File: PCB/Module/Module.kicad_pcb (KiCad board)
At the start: 2 copper layers, 30 x 30 mm, 22 parts, among them J1 SWD_Programmer, U1 PY32F002BF15P6TU, U2 PinHeaderTop, U3 PinHeaderRight, U4 PinHeaderBottom, U5 PinHeaderLeft, U6 Button

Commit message: Prevent accidental short circuit and add basic box 3d model freecad
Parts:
- moved R1 0.20 mm to (145.5, 91.2)
- moved R2 0.20 mm to (154.5, 91.2)
- moved R5 0.20 mm to (154.5, 108.8)
- moved R6 0.20 mm to (145.5, 108.8)
- moved R3 0.20 mm to (158.8, 95.5)
- moved R4 0.20 mm to (158.8, 104.5)
- moved R7 0.20 mm to (141.2, 104.5)
- moved R8 0.20 mm to (141.2, 95.5)
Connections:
- U2 pad 1: GND -> +5V
- U2 pad 2: +5V -> /DataTop1
- U2 pad 3: /DataTop1 -> GND
- U2 pad 4: /DataTop2 -> GND
- U2 pad 5: +5V -> /DataTop2
- U2 pad 6: GND -> +5V
- U3 pad 1: GND -> +5V
- U3 pad 2: +5V -> /DataRight1
- U3 pad 3: /DataRight1 -> GND
- U3 pad 4: /DataRight2 -> GND
- U3 pad 5: +5V -> /DataRight2
- U3 pad 6: GND -> +5V
- U4 pad 1: GND -> +5V
- U4 pad 2: +5V -> /DataBottom1
- U4 pad 3: /DataBottom1 -> GND
- U4 pad 4: /DataBottom2 -> GND
- U4 pad 5: +5V -> /DataBottom2
- U4 pad 6: GND -> +5V
- U5 pad 1: GND -> +5V
- U5 pad 2: +5V -> /DataLeft1
- U5 pad 3: /DataLeft1 -> GND
- U5 pad 4: /DataLeft2 -> GND
- U5 pad 5: +5V -> /DataLeft2
- U5 pad 6: GND -> +5V
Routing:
- net GND: track 37.3 -> 19.3 mm, vias 2 -> 5
- net +5V: track 14.3 -> 17.8 mm
- net /DataRight2: track 12.3 -> 11.8 mm
- net /DataRight1: track 12.3 -> 11.8 mm

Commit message: Update PCB
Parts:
- removed R9: 10k, Resistor_SMD:R_0402_1005Metric
- removed U6: Button, CustomFootprints:Button
- added J2: Shield_Connector_Top_Right, Connector_PinSocket_2.54mm:PinSocket_1x01_P2.54mm_Vertical, F.Cu at (161.0, 89.0)
- added J3: Shield_Connector_Bottom_Right, Connector_PinSocket_2.54mm:PinSocket_1x01_P2.54mm_Vertical, F.Cu at (161.0, 111.0)
- added J4: Shield_Connector_Top_Left, Connector_PinSocket_2.54mm:PinSocket_1x01_P2.54mm_Vertical, F.Cu at (139.0, 89.0)
- added J5: Shield_Connector_Bottom_Left, Connector_PinSocket_2.54mm:PinSocket_1x01_P2.54mm_Vertical, F.Cu at (139.0, 111.0)
- LED1, LED2, LED3, LED4: value LED-WS2812B -> SK6812MINI-HS; footprint CustomFootprints:LED-WS2812B -> CustomFootprints:LED-SK6812MINI-HS
- moved C1 16.1 mm to (145.3, 95.2), turned to 180 degrees
- moved R1 2.34 mm to (145.7, 93.5)
- moved R2 2.34 mm to (154.3, 93.5)
- moved R3 2.34 mm to (156.5, 95.7)
- moved R4 2.34 mm to (156.5, 104.3)
- moved U2 2.34 mm to (150.0, 91.5)
- moved U3 2.34 mm to (158.5, 100.0)
- moved U4 2.34 mm to (150.0, 108.5)
- moved U5 2.34 mm to (141.5, 100.0)
- moved R7 2.04 mm to (143.2, 104.3)
- moved R8 2.04 mm to (143.2, 95.7)
- moved R5 2.01 mm to (154.3, 106.8)
- moved R6 2.01 mm to (145.7, 106.8)
- moved C2 1.75 mm to (154.1, 105.1)
- moved LED2 1.10 mm to (155.4, 100.0), turned to 90 degrees
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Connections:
- LED1 pad 1: +5V -> GND
- LED1 pad 2: Net-(LED1-DOU) -> /LedIn
- LED1 pad 3: GND -> +5V
- LED1 pad 4: /LedIn -> Net-(LED1-DOUT)
- LED2 pad 1: +5V -> GND
- LED2 pad 2: Net-(LED2-DOU) -> Net-(LED1-DOUT)
- LED2 pad 3: GND -> +5V
- LED2 pad 4: Net-(LED1-DOU) -> Net-(LED2-DOUT)
- LED3 pad 1: +5V -> GND
- LED3 pad 2: Net-(LED3-DOU) -> Net-(LED2-DOUT)
- LED3 pad 3: GND -> +5V
- LED3 pad 4: Net-(LED2-DOU) -> Net-(LED3-DOUT)
- LED4 pad 1: +5V -> GND
- LED4 pad 2: unconnected-(LED4-DOU-Pad2) -> Net-(LED3-DOUT)
- LED4 pad 3: GND -> +5V
- LED4 pad 4: Net-(LED3-DOU) -> unconnected-(LED4-DOUT-Pad4)
- U1 pad 10: /DataRight1 -> /ShieldBottomRight
- U1 pad 12: unconnected-(U1-PB3-Pad12) -> /DataRight1
- U1 pad 13: unconnected-(U1-PB2-Pad13) -> /ShieldTopRight
- U1 pad 19: /ButtonRead -> /ShieldTopLeft
- U1 pad 2: unconnected-(U1-PA6-Pad2) -> /ShieldBottomLeft
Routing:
- net +5V: track 17.8 -> 87.3 mm, vias 2 -> 1
- net Net-(LED3-DOUT): track 0.00 -> 31.1 mm
- net Net-(LED2-DOUT): track 0.00 -> 31.0 mm
- net Net-(LED1-DOUT): track 0.00 -> 30.9 mm
- net /ShieldTopRight: track 0.00 -> 13.4 mm
- net /ShieldTopLeft: track 0.00 -> 13.1 mm
- net /ShieldBottomRight: track 0.00 -> 12.8 mm
- net /ShieldBottomLeft: track 0.00 -> 12.7 mm
- net /ButtonRead: track 10.7 -> 0.00 mm
- net Net-(LED1-DOU): track 8.95 -> 0.00 mm
- net Net-(LED3-DOU): track 8.95 -> 0.00 mm
- net GND: track 19.3 -> 12.2 mm, vias 5 -> 3
- net /DataLeft2: track 12.7 -> 5.96 mm
- net Net-(LED2-DOU): track 6.54 -> 0.00 mm
- net /DataLeft1: track 12.0 -> 5.96 mm
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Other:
- board size 30 x 30 mm -> 34.2 x 34.2 mm
- board text added: "+5V"
- board text added: "GND"
- board text added: "PCB"
- board text added: "Pogo Pins"
- board text added: "RST"
- board text added: "SWC"
- board text added: "SWD"

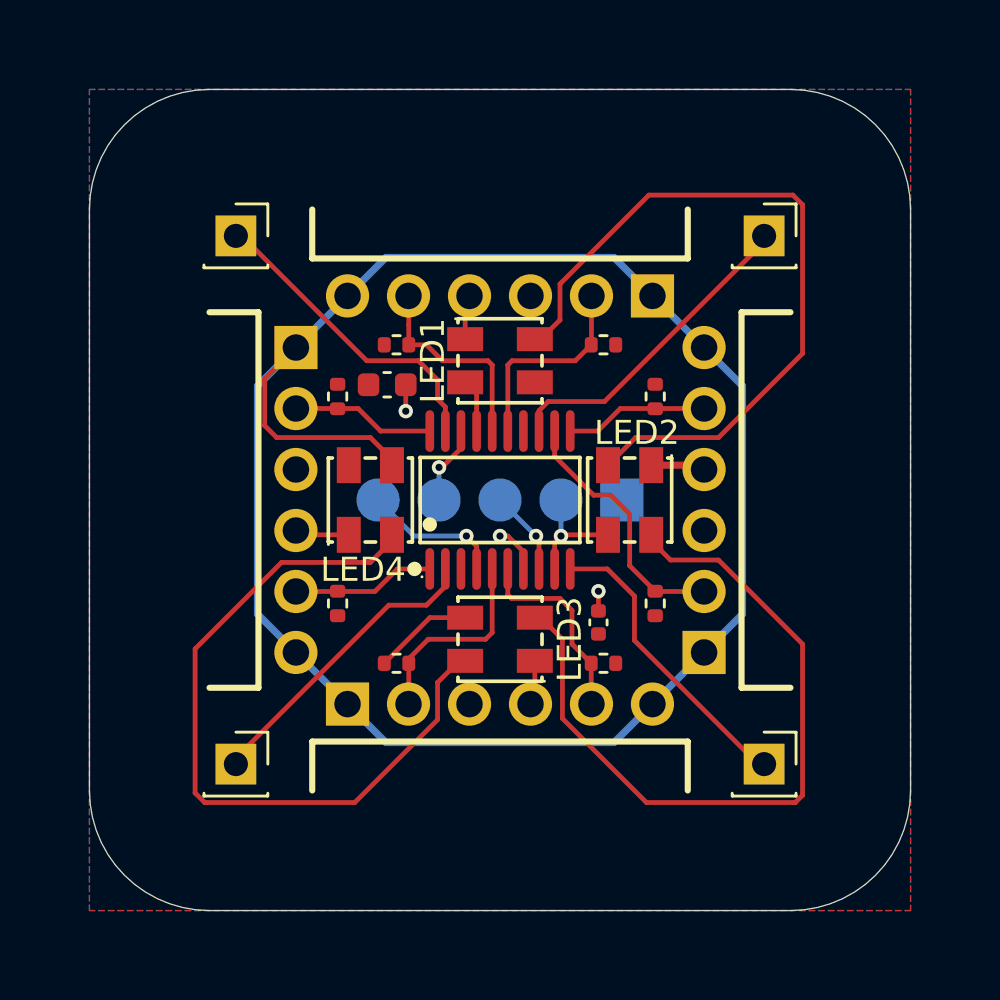
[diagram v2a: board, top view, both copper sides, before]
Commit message: Add hall sensor shield
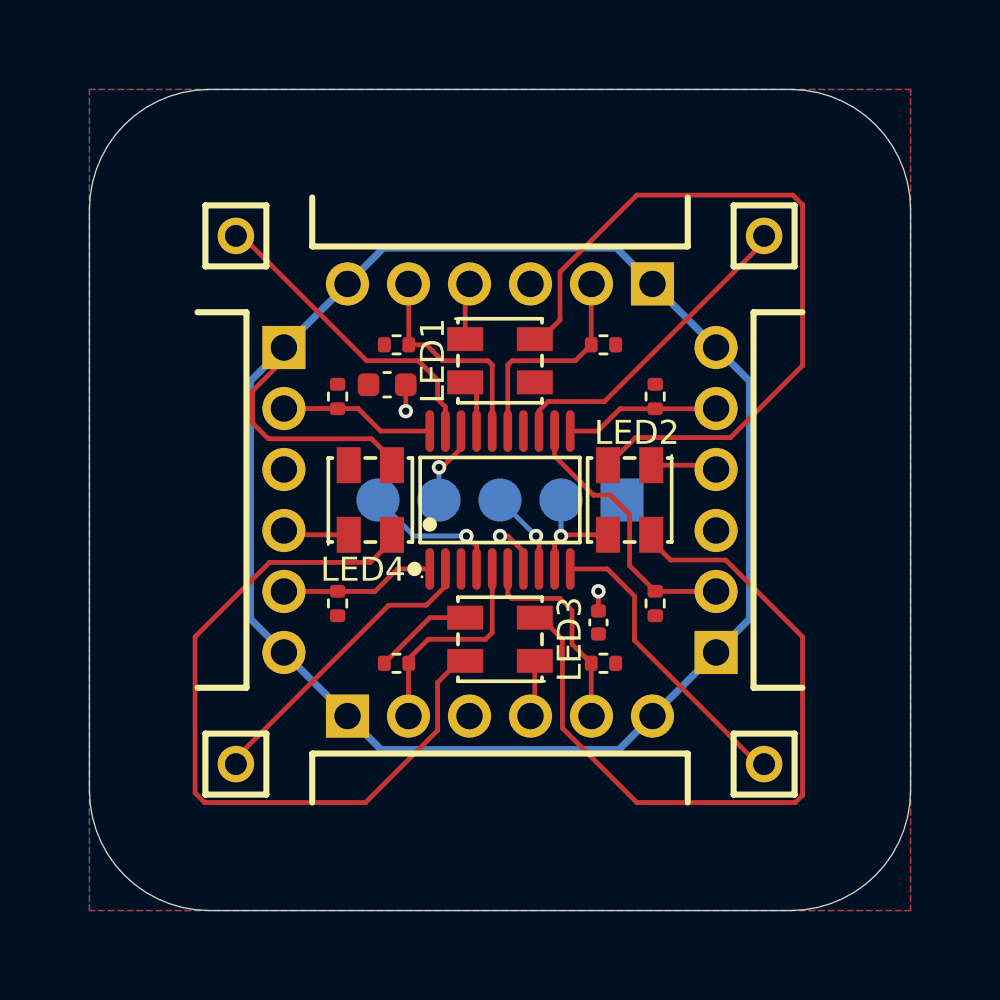
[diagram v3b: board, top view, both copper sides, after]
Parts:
- J2, J3, J4, J5: footprint Connector_PinSocket_2.54mm:PinSocket_1x01_P2.54mm_Vertical -> CustomFootprints:HDR-TH_1P-V-F-1
- moved U2 0.50 mm to (150.0, 91.0)
- moved U3 0.50 mm to (159.0, 100.0)
- moved U4 0.50 mm to (150.0, 109.0)
- moved U5 0.50 mm to (141.0, 100.0)
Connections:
- net /ShieldBottomLeft renamed /ShieldBottomLeft_ADC
- net /ShieldTopLeft renamed /ShieldTopLeft_ADC
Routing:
- net +5V: track 87.3 -> 90.2 mm
- net GND: track 12.2 -> 13.2 mm
- net /DataTop2: track 8.62 -> 9.62 mm
- net Net-(LED1-DOUT): track 30.9 -> 31.5 mm
- net Net-(LED3-DOUT): track 31.1 -> 31.6 mm
- net /DataTop1: track 8.62 -> 9.13 mm
- net /DataRight2: track 5.96 -> 6.47 mm
- net /DataRight1: track 10.9 -> 11.4 mm
- net /DataLeft2: track 5.96 -> 6.46 mm
- net /DataLeft1: track 5.96 -> 6.46 mm

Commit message: Add smart cube panel
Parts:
- added REF**: Tab, PCM_kikit:Tab, F.Cu at (150.0, 82.7)
- added REF**: Tab, PCM_kikit:Tab, F.Cu at (150.0, 117.3)
- added REF**: Tab, PCM_kikit:Tab, F.Cu at (132.7, 100.0)
- added REF**: Tab, PCM_kikit:Tab, F.Cu at (167.3, 100.0)

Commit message: Fix 3d model paths
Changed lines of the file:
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@@
 			)
 		)
-		(pad "1" thru_hole rect
+		(pad "1" thru_hole oval
 			(at -6.350013 0 180)
 			(size 1.8 1.8)
@@
 			(pintype "passive")
 		)
-		(pad "3" thru_hole circle
+		(pad "3" thru_hole rect
 			(at -1.270003 0 180)
 			(size 1.8 1.8)
@@
 			(pintype "passive")
 		)
-		(pad "4" thru_hole circle
+		(pad "4" thru_hole rect
 			(at 1.270003 0 180)
 			(size 1.8 1.8)
@@
 			(pintype "passive")
 		)
-		(model "./packages3d/HDR-TH_6P-P2.54-H-M-W10.4.step"
+		(model "${KIPRJMOD}/../lib/CustomFootprints.pretty/packages3d/HDR-TH_6P-P2.54-H-M-W10.4.step"
 			(offset
 				(xyz 0 -2.850003 0.000006)
@@
 			(pintype "passive")
 		)
-		(model "./packages3d/HDR-TH_1P-V-F-1.step"
+		(model "${KIPRJMOD}/../lib/CustomFootprints.pretty/packages3d/HDR-TH_1P-V-F-1.step"
 			(offset
 				(xyz 0 0 0)
@@
 			)
 		)
-		(pad "1" thru_hole rect
+		(pad "1" thru_hole oval
 			(at -6.350013 0 90)
 			(size 1.8 1.8)
@@
 			(pintype "passive")
 		)
-		(pad "3" thru_hole circle
+		(pad "3" thru_hole rect
 			(at -1.270003 0 90)
 			(size 1.8 1.8)
@@
 			(pintype "passive")
 		)
-		(pad "4" thru_hole circle
+		(pad "4" thru_hole rect
 			(at 1.270003 0 90)
 			(size 1.8 1.8)
@@
 			(pintype "passive")
 		)
-		(model "./packages3d/HDR-TH_6P-P2.54-H-M-W10.4.step"
+		(model "${KIPRJMOD}/../lib/CustomFootprints.pretty/packages3d/HDR-TH_6P-P2.54-H-M-W10.4.step"
 			(offset
 				(xyz 0 -2.850003 0.000006)
@@
 			)
 		)
-		(pad "1" thru_hole rect
+		(pad "1" thru_hole oval
 			(at -6.350013 0 270)
 			(size 1.8 1.8)
@@
 			(pintype "passive")
 		)
-		(pad "3" thru_hole circle
+		(pad "3" thru_hole rect
 			(at -1.270003 0 270)
 			(size 1.8 1.8)
@@
 			(pintype "passive")
 		)
-		(pad "4" thru_hole circle
+		(pad "4" thru_hole rect
 			(at 1.270003 0 270)
 			(size 1.8 1.8)
@@
 			(pintype "passive")
 		)
-		(model "./packages3d/HDR-TH_6P-P2.54-H-M-W10.4.step"
+		(model "${KIPRJMOD}/../lib/CustomFootprints.pretty/packages3d/HDR-TH_6P-P2.54-H-M-W10.4.step"
 			(offset
 				(xyz 0 -2.850003 0.000006)
@@
 			(pintype "output")
 		)
-		(model "./packages3d/LED-SMD_4P-L3.5-W3.5-BR_SK6812MINI-HS.step"
+		(model "${KIPRJMOD}/../lib/CustomFootprints.pretty/packages3d/LED-SMD_4P-L3.5-W3.5-BR_SK6812MINI-HS.step"
 			(offset
 				(xyz 0.0000507999992371 0.0000507999992371 0)
@@
 			(pintype "output")
 		)
-		(model "./packages3d/LED-SMD_4P-L3.5-W3.5-BR_SK6812MINI-HS.step"
+		(model "${KIPRJMOD}/../lib/CustomFootprints.pretty/packages3d/LED-SMD_4P-L3.5-W3.5-BR_SK6812MINI-HS.step"
 			(offset
 				(xyz 0.0000507999992371 0.0000507999992371 0)
@@
 			(pintype "output+no_connect")
 		)
-		(model "./packages3d/LED-SMD_4P-L3.5-W3.5-BR_SK6812MINI-HS.step"
+		(model "${KIPRJMOD}/../lib/CustomFootprints.pretty/packages3d/LED-SMD_4P-L3.5-W3.5-BR_SK6812MINI-HS.step"
 			(offset
 				(xyz 0.0000507999992371 0.0000507999992371 0)
@@
 			)
 		)
-		(pad "1" thru_hole rect
+		(pad "1" thru_hole oval
 			(at -6.350013 0)
 			(size 1.8 1.8)
@@
 			(pintype "passive")
 		)
-		(pad "3" thru_hole circle
+		(pad "3" thru_hole rect
 			(at -1.270003 0)
 			(size 1.8 1.8)
@@
 			(pintype "passive")
 		)
-		(pad "4" thru_hole circle
+		(pad "4" thru_hole rect
 			(at 1.270003 0)
 			(size 1.8 1.8)
@@
 			(pintype "passive")
 		)
-		(model "./packages3d/HDR-TH_6P-P2.54-H-M-W10.4.step"
+		(model "${KIPRJMOD}/../lib/CustomFootprints.pretty/packages3d/HDR-TH_6P-P2.54-H-M-W10.4.step"
 			(offset
 				(xyz 0 -2.850003 0.000006)
@@
 			(pintype "passive")
 		)
-		(model "./packages3d/HDR-TH_1P-V-F-1.step"
+		(model "${KIPRJMOD}/../lib/CustomFootprints.pretty/packages3d/HDR-TH_1P-V-F-1.step"
 			(offset
 				(xyz 0 0 0)
@@
 			(pintype "passive")
 		)
-		(model "./packages3d/HDR-TH_1P-V-F-1.step"
+		(model "${KIPRJMOD}/../lib/CustomFootprints.pretty/packages3d/HDR-TH_1P-V-F-1.step"
 			(offset
 				(xyz 0 0 0)
@@
 			(pintype "bidirectional")
 		)
-		(model "./packages3d/TSSOP-20_L6.5-W4.4-P0.65-LS6.4-BL.step"
+		(model "${KIPRJMOD}/../lib/CustomFootprints.pretty/packages3d/TSSOP-20_L6.5-W4.4-P0.65-LS6.4-BL.step"
 			(offset
 				(xyz 0 0 0)
@@
 			(pintype "passive")
 		)
-		(model "./packages3d/HDR-TH_1P-V-F-1.step"
+		(model "${KIPRJMOD}/../lib/CustomFootprints.pretty/packages3d/HDR-TH_1P-V-F-1.step"
 			(offset
 				(xyz 0 0 0)
@@
 			(pintype "output")
 		)
-		(model "./packages3d/LED-SMD_4P-L3.5-W3.5-BR_SK6812MINI-HS.step"
+		(model "${KIPRJMOD}/../lib/CustomFootprints.pretty/packages3d/LED-SMD_4P-L3.5-W3.5-BR_SK6812MINI-HS.step"
 			(offset
 				(xyz 0.0000507999992371 0.0000507999992371 0)
